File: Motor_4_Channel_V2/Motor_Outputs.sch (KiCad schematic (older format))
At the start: 36 parts

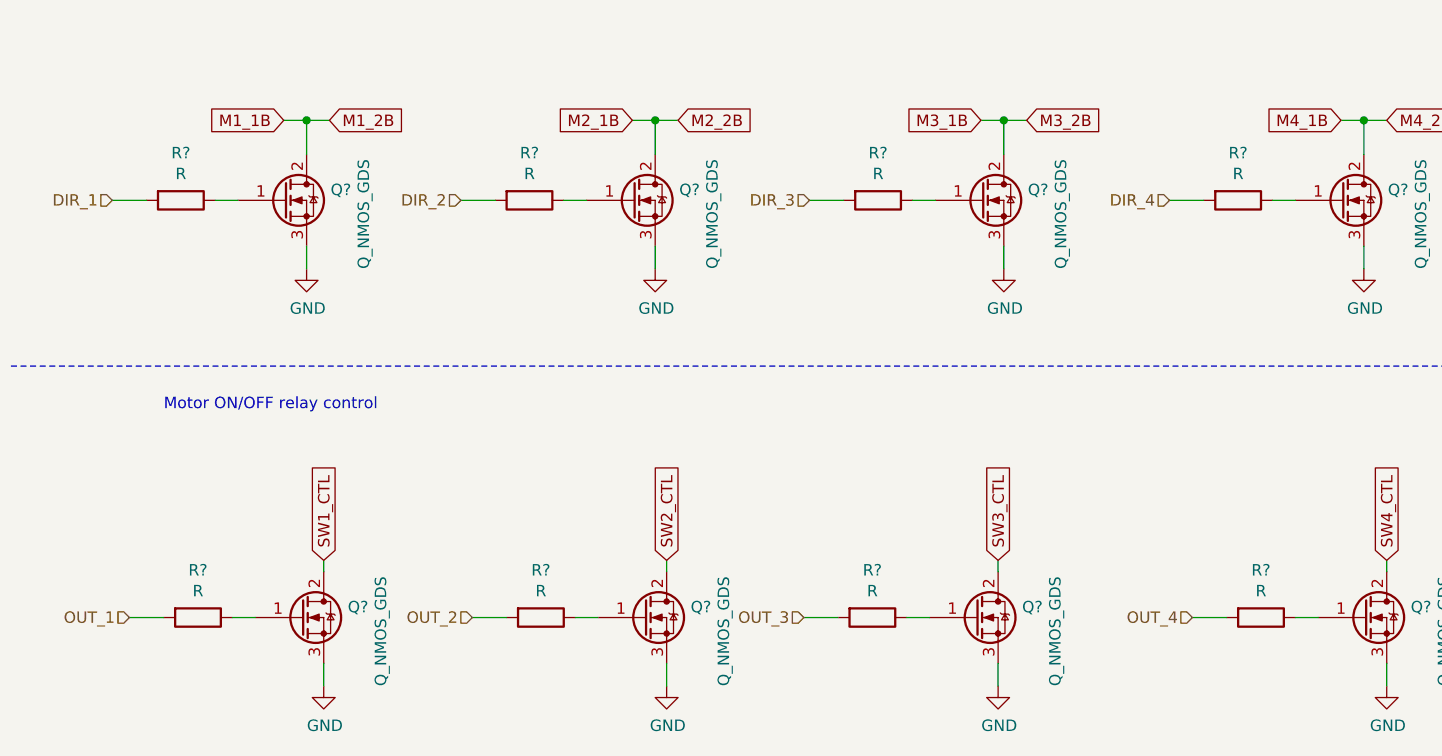
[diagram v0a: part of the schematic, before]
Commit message: Added power circuit for NRF52. Added SMT Practice V1 project. Modified Motor v2 project.
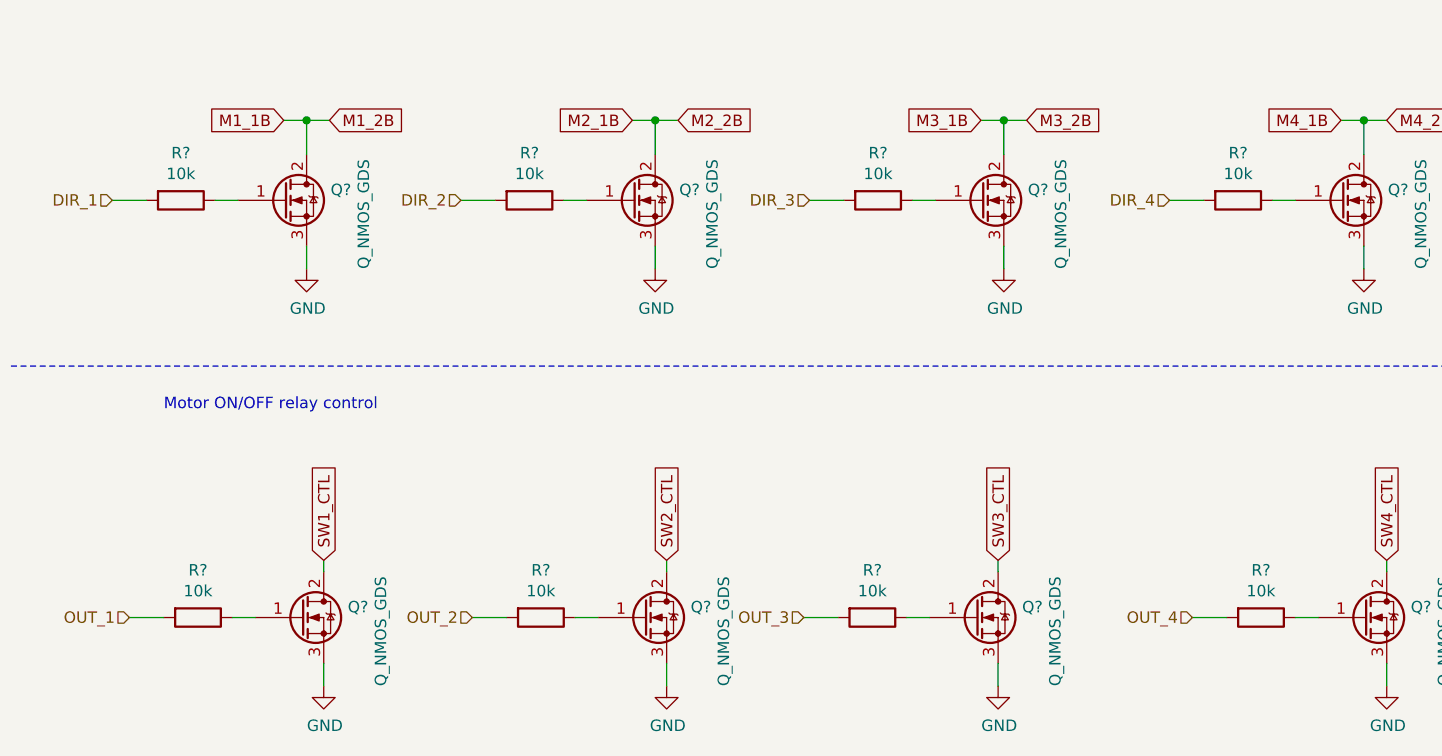
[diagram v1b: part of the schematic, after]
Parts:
- Q? (x8): footprint (none) -> Package_TO_SOT_SMD:SOT-23
- R? (x8): value R -> 10k; footprint (none) -> Resistor_SMD:R_0603_1608Metric_Pad1.05x0.95mm_HandSolder
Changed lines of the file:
@@
 F 0 "Q?" H 1955 7046 50  0000 L CNN
 F 1 "Q_NMOS_GDS" V 2100 6700 50  0000 L CNN
-F 2 "" H 1950 7100 50  0001 C CNN
+F 2 "Package_TO_SOT_SMD:SOT-23" H 1950 7100 50  0001 C CNN
 F 3 "~" H 1750 7000 50  0001 C CNN
 	1    1750 7000
@@
 AR Path="/5C130376/5C139370" Ref="R?"  Part="1"
 F 0 "R?" V 1093 7000 50  0000 C CNN
-F 1 "R" V 1184 7000 50  0000 C CNN
-F 2 "" V 1230 7000 50  0001 C CNN
+F 1 "10k" V 1184 7000 50  0000 C CNN
+F 2 "Resistor_SMD:R_0603_1608Metric_Pad1.05x0.95mm_HandSolder" V 1230 7000 50  0001 C CNN
 F 3 "~" H 1300 7000 50  0001 C CNN
 	1    1300 7000
@@
 F 0 "Q?" H 3455 7046 50  0000 L CNN
 F 1 "Q_NMOS_GDS" V 3600 6700 50  0000 L CNN
-F 2 "" H 3450 7100 50  0001 C CNN
+F 2 "Package_TO_SOT_SMD:SOT-23" H 3450 7100 50  0001 C CNN
 F 3 "~" H 3250 7000 50  0001 C CNN
 	1    3250 7000
@@
 AR Path="/5C130376/5C139380" Ref="R?"  Part="1"
 F 0 "R?" V 2593 7000 50  0000 C CNN
-F 1 "R" V 2684 7000 50  0000 C CNN
-F 2 "" V 2730 7000 50  0001 C CNN
+F 1 "10k" V 2684 7000 50  0000 C CNN
+F 2 "Resistor_SMD:R_0603_1608Metric_Pad1.05x0.95mm_HandSolder" V 2730 7000 50  0001 C CNN
 F 3 "~" H 2800 7000 50  0001 C CNN
 	1    2800 7000
@@
 F 0 "Q?" H 4905 7046 50  0000 L CNN
 F 1 "Q_NMOS_GDS" V 5050 6700 50  0000 L CNN
-F 2 "" H 4900 7100 50  0001 C CNN
+F 2 "Package_TO_SOT_SMD:SOT-23" H 4900 7100 50  0001 C CNN
 F 3 "~" H 4700 7000 50  0001 C CNN
 	1    4700 7000
@@
 AR Path="/5C130376/5C139390" Ref="R?"  Part="1"
 F 0 "R?" V 4043 7000 50  0000 C CNN
-F 1 "R" V 4134 7000 50  0000 C CNN
-F 2 "" V 4180 7000 50  0001 C CNN
+F 1 "10k" V 4134 7000 50  0000 C CNN
+F 2 "Resistor_SMD:R_0603_1608Metric_Pad1.05x0.95mm_HandSolder" V 4180 7000 50  0001 C CNN
 F 3 "~" H 4250 7000 50  0001 C CNN
 	1    4250 7000
@@
 F 0 "Q?" H 6605 7046 50  0000 L CNN
 F 1 "Q_NMOS_GDS" V 6750 6700 50  0000 L CNN
-F 2 "" H 6600 7100 50  0001 C CNN
+F 2 "Package_TO_SOT_SMD:SOT-23" H 6600 7100 50  0001 C CNN
 F 3 "~" H 6400 7000 50  0001 C CNN
 	1    6400 7000
@@
 AR Path="/5C130376/5C1393A0" Ref="R?"  Part="1"
 F 0 "R?" V 5743 7000 50  0000 C CNN
-F 1 "R" V 5834 7000 50  0000 C CNN
-F 2 "" V 5880 7000 50  0001 C CNN
+F 1 "10k" V 5834 7000 50  0000 C CNN
+F 2 "Resistor_SMD:R_0603_1608Metric_Pad1.05x0.95mm_HandSolder" V 5880 7000 50  0001 C CNN
 F 3 "~" H 5950 7000 50  0001 C CNN
 	1    5950 7000
@@
 F 0 "Q?" H 4930 5221 50  0000 L CNN
 F 1 "Q_NMOS_GDS" V 5075 4875 50  0000 L CNN
-F 2 "" H 4925 5275 50  0001 C CNN
+F 2 "Package_TO_SOT_SMD:SOT-23" H 4925 5275 50  0001 C CNN
 F 3 "~" H 4725 5175 50  0001 C CNN
 	1    4725 5175
@@
 F 0 "Q?" H 6505 5221 50  0000 L CNN
 F 1 "Q_NMOS_GDS" V 6650 4875 50  0000 L CNN
-F 2 "" H 6500 5275 50  0001 C CNN
+F 2 "Package_TO_SOT_SMD:SOT-23" H 6500 5275 50  0001 C CNN
 F 3 "~" H 6300 5175 50  0001 C CNN
 	1    6300 5175
@@
 AR Path="/5C130376/5C13B576" Ref="R?"  Part="1"
 F 0 "R?" V 4068 5175 50  0000 C CNN
-F 1 "R" V 4159 5175 50  0000 C CNN
-F 2 "" V 4205 5175 50  0001 C CNN
+F 1 "10k" V 4159 5175 50  0000 C CNN
+F 2 "Resistor_SMD:R_0603_1608Metric_Pad1.05x0.95mm_HandSolder" V 4205 5175 50  0001 C CNN
 F 3 "~" H 4275 5175 50  0001 C CNN
 	1    4275 5175
@@
 AR Path="/5C130376/5C13B57D" Ref="R?"  Part="1"
 F 0 "R?" V 5643 5175 50  0000 C CNN
-F 1 "R" V 5734 5175 50  0000 C CNN
-F 2 "" V 5780 5175 50  0001 C CNN
+F 1 "10k" V 5734 5175 50  0000 C CNN
+F 2 "Resistor_SMD:R_0603_1608Metric_Pad1.05x0.95mm_HandSolder" V 5780 5175 50  0001 C CNN
 F 3 "~" H 5850 5175 50  0001 C CNN
 	1    5850 5175
@@
 F 0 "Q?" H 1880 5221 50  0000 L CNN
 F 1 "Q_NMOS_GDS" V 2025 4875 50  0000 L CNN
-F 2 "" H 1875 5275 50  0001 C CNN
+F 2 "Package_TO_SOT_SMD:SOT-23" H 1875 5275 50  0001 C CNN
 F 3 "~" H 1675 5175 50  0001 C CNN
 	1    1675 5175
@@
 F 0 "Q?" H 3405 5221 50  0000 L CNN
 F 1 "Q_NMOS_GDS" V 3550 4875 50  0000 L CNN
-F 2 "" H 3400 5275 50  0001 C CNN
+F 2 "Package_TO_SOT_SMD:SOT-23" H 3400 5275 50  0001 C CNN
 F 3 "~" H 3200 5175 50  0001 C CNN
 	1    3200 5175
@@
 AR Path="/5C130376/5C13D901" Ref="R?"  Part="1"
 F 0 "R?" V 1018 5175 50  0000 C CNN
-F 1 "R" V 1109 5175 50  0000 C CNN
-F 2 "" V 1155 5175 50  0001 C CNN
+F 1 "10k" V 1109 5175 50  0000 C CNN
+F 2 "Resistor_SMD:R_0603_1608Metric_Pad1.05x0.95mm_HandSolder" V 1155 5175 50  0001 C CNN
 F 3 "~" H 1225 5175 50  0001 C CNN
 	1    1225 5175
@@
 AR Path="/5C130376/5C13D908" Ref="R?"  Part="1"
 F 0 "R?" V 2543 5175 50  0000 C CNN
-F 1 "R" V 2634 5175 50  0000 C CNN
-F 2 "" V 2680 5175 50  0001 C CNN
+F 1 "10k" V 2634 5175 50  0000 C CNN
+F 2 "Resistor_SMD:R_0603_1608Metric_Pad1.05x0.95mm_HandSolder" V 2680 5175 50  0001 C CNN
 F 3 "~" H 2750 5175 50  0001 C CNN
 	1    2750 5175

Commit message: Added digikey library. Started PCB layout for Motor 4 CH V2.
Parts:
- D1, D10, D11, D12, D2, D3, D4, D5, D6, D7, D8, D9: renamed from D?; footprint (none) -> digikey-footprints:DO-214AC
- K1, K2, K3, K4: renamed from K?; value FINDER-32.21-x300 -> G8N-1L-DC12; footprint Relay_THT:Relay_SPST_Finder_32.21-x300 -> Custom_Footprints:G8N-1L-DC12; symbol Relay:FINDER-32.21-x300 -> Project_Libary:G8N-1L-DC12
- U12, U13, U14, U15: renamed from U?; footprint (none) -> Custom_Footprints:G8NW-2H-DC12
- gave numbers to parts that had none: 16
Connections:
- wire segments 191 -> 203
- no-connect marks 0 -> 4

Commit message: Added progress to Motor 4 CH V2 layout.
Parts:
- Q1, Q2, Q3, Q4, Q5, Q6, Q7, Q8: symbol Device:Q_NMOS_GDS -> Device:Q_NMOS_GSD
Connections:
- net GND: now also Q1.2 (S), Q2.2 (S), Q3.2 (S), Q4.2 (S), Q5.2 (S), Q6.2 (S), Q7.2 (S), Q8.2 (S); no longer Q1.3 (S), Q2.3 (S), Q3.3 (S), Q4.3 (S), Q5.3 (S), Q6.3 (S), Q7.3 (S), Q8.3 (S), U12.4 (IN2_NC), U12.8 (IN1_NO), U13.4 (IN2_NC), U13.8 (IN1_NO), U14.4 (IN2_NC), U14.8 (IN1_NO), U15.4 (IN2_NC), U15.8 (IN1_NO)
- net M1_1B: now also Q1.3 (D); no longer Q1.2 (D)
- net M2_1B: now also Q3.3 (D); no longer Q3.2 (D)
- net M3_1B: now also Q6.3 (D); no longer Q6.2 (D)
- net M4_1B: now also Q7.3 (D); no longer Q7.2 (D)
- net SW1_CTL: now also Q2.3 (D); no longer Q2.2 (D)
- net SW2_CTL: now also Q4.3 (D); no longer Q4.2 (D)
- net SW3_CTL: now also Q5.3 (D); no longer Q5.2 (D)
- net SW4_CTL: now also Q8.3 (D); no longer Q8.2 (D)
- new net: U12.4 (IN2_NC), U12.8 (IN1_NO)
- new net: U13.4 (IN2_NC), U13.8 (IN1_NO)
- new net: U14.4 (IN2_NC), U14.8 (IN1_NO)
- new net: U15.4 (IN2_NC), U15.8 (IN1_NO)
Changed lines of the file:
@@
-	1    0    0    -1
-$EndComp
-$Comp
-L power:GND #PWR?
-U 1 1 5C1392EC
-P 2050 2550
-AR Path="/5C1392EC" Ref="#PWR?"  Part="1"
-AR Path="/5C130376/5C1392EC" Ref="#PWR032"  Part="1"
-F 0 "#PWR032" H 2050 2300 50  0001 C CNN
-F 1 "GND" H 2055 2377 50  0000 C CNN
-F 2 "" H 2050 2550 50  0001 C CNN
-F 3 "" H 2050 2550 50  0001 C CNN
-	1    2050 2550
 	1    0    0    -1
 $EndComp
@@
 	1950 2400 1950 2550
 Wire Wire Line
-	1950 2550 2050 2550
-Wire Wire Line
 	2150 2400 2150 2550
 Wire Wire Line
-	2150 2550 2050 2550
-Connection ~ 2050 2550
-$Comp
-L power:GND #PWR?
-U 1 1 5C1392F7
-P 4550 2550
-AR Path="/5C1392F7" Ref="#PWR?"  Part="1"
-AR Path="/5C130376/5C1392F7" Ref="#PWR035"  Part="1"
-F 0 "#PWR035" H 4550 2300 50  0001 C CNN
-F 1 "GND" H 4555 2377 50  0000 C CNN
-F 2 "" H 4550 2550 50  0001 C CNN
-F 3 "" H 4550 2550 50  0001 C CNN
-	1    4550 2550
-	1    0    0    -1
-$EndComp
-Wire Wire Line
 	4450 2400 4450 2550
 Wire Wire Line
-	4450 2550 4550 2550
-Wire Wire Line
 	4650 2400 4650 2550
 Wire Wire Line
-	4650 2550 4550 2550
-Connection ~ 4550 2550
-$Comp
-L power:GND #PWR?
-U 1 1 5C139302
-P 7150 2550
-AR Path="/5C139302" Ref="#PWR?"  Part="1"
-AR Path="/5C130376/5C139302" Ref="#PWR040"  Part="1"
-F 0 "#PWR040" H 7150 2300 50  0001 C CNN
-F 1 "GND" H 7155 2377 50  0000 C CNN
-F 2 "" H 7150 2550 50  0001 C CNN
-F 3 "" H 7150 2550 50  0001 C CNN
-	1    7150 2550
-	1    0    0    -1
-$EndComp
-Wire Wire Line
 	7050 2400 7050 2550
 Wire Wire Line
-	7050 2550 7150 2550
-Wire Wire Line
 	7250 2400 7250 2550
 Wire Wire Line
-	7250 2550 7150 2550
-Connection ~ 7150 2550
-$Comp
-L power:GND #PWR?
-U 1 1 5C13930D
-P 9700 2550
-AR Path="/5C13930D" Ref="#PWR?"  Part="1"
-AR Path="/5C130376/5C13930D" Ref="#PWR041"  Part="1"
-F 0 "#PWR041" H 9700 2300 50  0001 C CNN
-F 1 "GND" H 9705 2377 50  0000 C CNN
-F 2 "" H 9700 2550 50  0001 C CNN
-F 3 "" H 9700 2550 50  0001 C CNN
-	1    9700 2550
-	1    0    0    -1
-$EndComp
-Wire Wire Line
 	9600 2400 9600 2550
 Wire Wire Line
-	9600 2550 9700 2550
-Wire Wire Line
 	9800 2400 9800 2550
-Wire Wire Line
-	9800 2550 9700 2550
-Connection ~ 9700 2550
 $Comp
 L Project_Libary:G8N-1L-DC12 K?
@@
 $EndComp
 $Comp
-L Device:Q_NMOS_GDS Q?
+L Device:Q_NMOS_GSD Q?
 U 1 1 5C139369
 P 1750 7000
@@
 	1150 7000 1000 7000
 $Comp
-L Device:Q_NMOS_GDS Q?
+L Device:Q_NMOS_GSD Q?
 U 1 1 5C139379
 P 3250 7000
@@
 	2650 7000 2500 7000
 $Comp
-L Device:Q_NMOS_GDS Q?
+L Device:Q_NMOS_GSD Q?
 U 1 1 5C139389
 P 4700 7000
@@
 	4100 7000 3950 7000
 $Comp
-L Device:Q_NMOS_GDS Q?
+L Device:Q_NMOS_GSD Q?
 U 1 1 5C139399
 P 6400 7000
@@
 	6500 6800 6500 6750
 $Comp
-L Device:Q_NMOS_GDS Q?
+L Device:Q_NMOS_GSD Q?
 U 1 1 5C13B55A
 P 4725 5175
@@
 $EndComp
 $Comp
-L Device:Q_NMOS_GDS Q?
+L Device:Q_NMOS_GSD Q?
 U 1 1 5C13B561
 P 6300 5175
@@
 	5700 5175 5550 5175
 $Comp
-L Device:Q_NMOS_GDS Q?
+L Device:Q_NMOS_GSD Q?
 U 1 1 5C13D8E5
 P 1675 5175
@@
 $EndComp
 $Comp
-L Device:Q_NMOS_GDS Q?
+L Device:Q_NMOS_GSD Q?
 U 1 1 5C13D8EC
 P 3200 5175
@@
 Wire Wire Line
 	8900 1650 8550 1650
+Wire Wire Line
+	1950 2550 2150 2550
+Wire Wire Line
+	4450 2550 4650 2550
+Wire Wire Line
+	7050 2550 7250 2550
+Wire Wire Line
+	9600 2550 9800 2550
 $EndSCHEMATC

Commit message: Misc. changes to Motor PCB.
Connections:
- net OUT_1+: now also U12.1 (OUT_2); no longer U12.6 (OUT_1)
- net OUT_1-: now also U12.6 (OUT_1); no longer U12.1 (OUT_2)
- net OUT_2+: now also U13.1 (OUT_2); no longer U13.6 (OUT_1)
- net OUT_2-: now also U13.6 (OUT_1); no longer U13.1 (OUT_2)
- net OUT_3+: now also U14.1 (OUT_2); no longer U14.6 (OUT_1)
- net OUT_3-: now also U14.6 (OUT_1); no longer U14.1 (OUT_2)
- net OUT_4+: now also U15.1 (OUT_2); no longer U15.6 (OUT_1)
- net OUT_4-: now also U15.6 (OUT_1); no longer U15.1 (OUT_2)
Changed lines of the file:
@@
 Wire Wire Line
 	1850 7300 1850 7200
+Text HLabel 2200 1400 1    50   Output ~ 0
+OUT_1+
 Text HLabel 1900 1400 1    50   Output ~ 0
-OUT_1+
-Text HLabel 2200 1400 1    50   Output ~ 0
 OUT_1-
+Text HLabel 4700 1400 1    50   Output ~ 0
+OUT_2+
 Text HLabel 4400 1400 1    50   Output ~ 0
-OUT_2+
-Text HLabel 4700 1400 1    50   Output ~ 0
 OUT_2-
+Text HLabel 7300 1400 1    50   Output ~ 0
+OUT_3+
 Text HLabel 7000 1400 1    50   Output ~ 0
-OUT_3+
-Text HLabel 7300 1400 1    50   Output ~ 0
 OUT_3-
+Text HLabel 9850 1400 1    50   Output ~ 0
+OUT_4+
 Text HLabel 9550 1400 1    50   Output ~ 0
-OUT_4+
-Text HLabel 9850 1400 1    50   Output ~ 0
 OUT_4-
 Text HLabel 925  5175 0    50   Input ~ 0
